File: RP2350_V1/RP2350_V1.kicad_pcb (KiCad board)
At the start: 4 copper layers, 65.3 x 95.8 mm, 102 parts, among them IC1 DMP1045U-7, IC2 DMP1045U-7, IC3 DMP1045U-7, J1 Conn_01x04_Pin, J2 Conn_01x08_Socket, J3 USB_C_Receptacle_USB2.0_16P, J4 Conn_01x08_Socket, J5 Conn_01x08_Socket, J6 Conn_01x02_Pin, J7 Conn_01x04_Pin, SW1 PTS 647 SN50 SMTR2 LFS, SW10 PTS 647 SN50 SMTR2 LFS, SW11 PTS 647 SN50 SMTR2 LFS, SW12 PTS 647 SN50 SMTR2 LFS, SW13 PTS 647 SN50 SMTR2 LFS, SW14 PTS 647 SN50 SMTR2 LFS, SW4 PTS 647 SN50 SMTR2 LFS, SW9 PTS 647 SN50 SMTR2 LFS, U1 RP2350_60QFN, U2 W25Q128JVS, U3 TPS628110AQWRWYRQ1, U4 MCP73812T-420I-OT, U5 TLV3012AIDBVR, U6 74HC14, Y1 ASE-12.000MHZ-ET

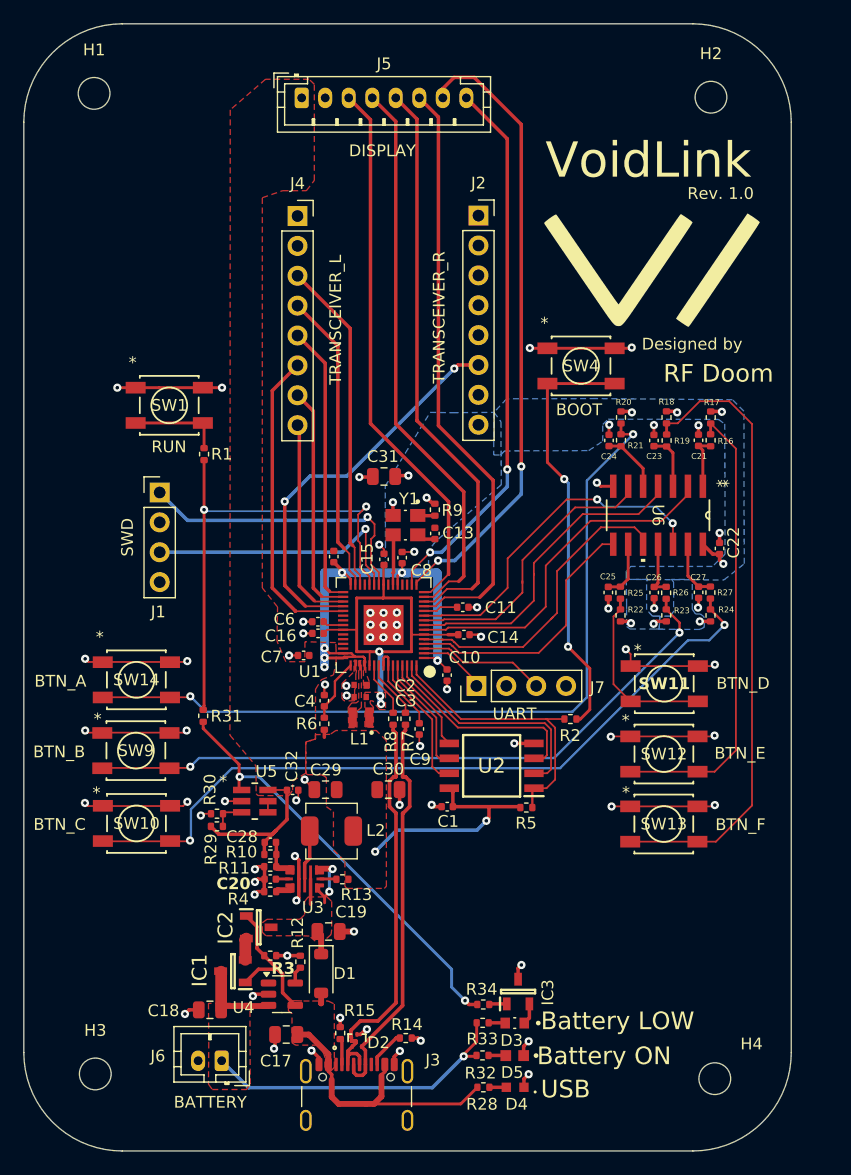
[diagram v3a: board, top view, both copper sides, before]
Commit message: sch updates, lay in progress
updated TLV3012 package,
changed cmos oscillator to xtal,
updated LCSC component values for all non-generic components
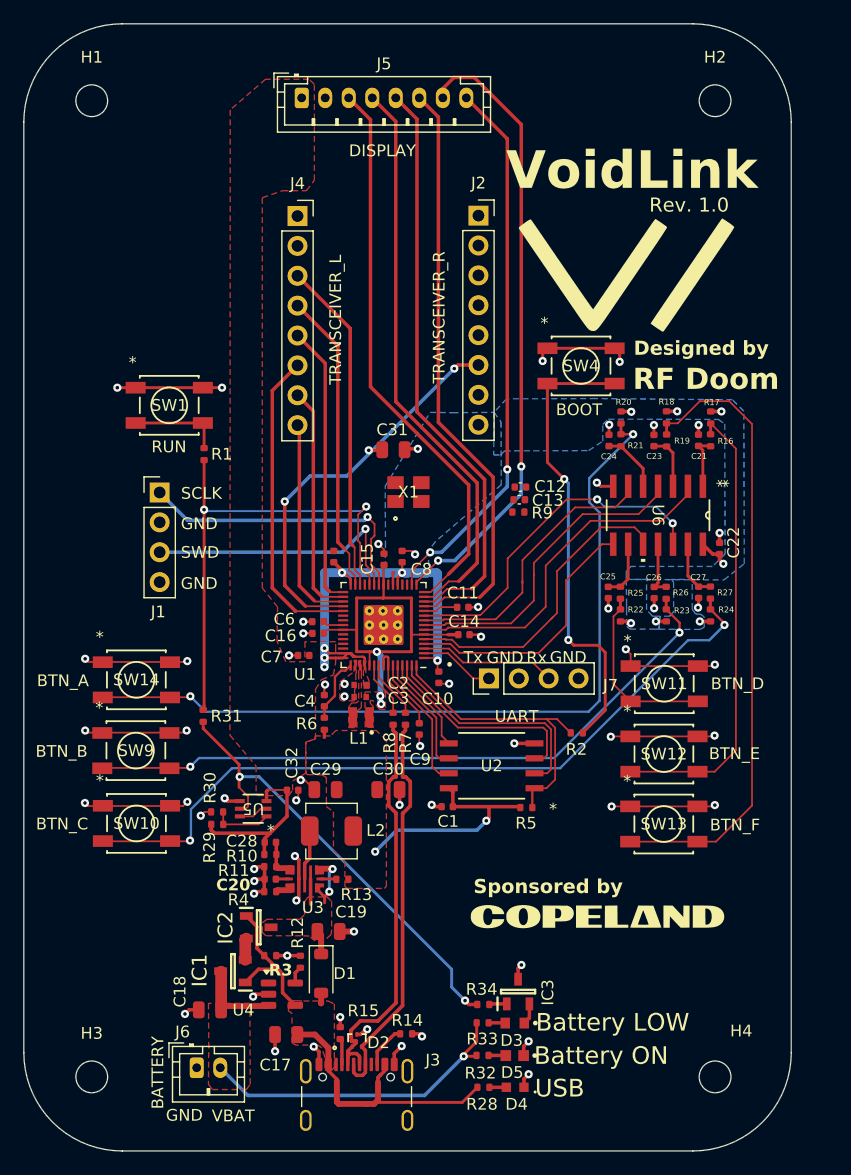
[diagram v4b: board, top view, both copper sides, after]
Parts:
- removed Y1: ASE-12.000MHZ-ET, My_Footprints:XTAL_ASE-12.000MHZ-ET
- added ?: , clipboard:0d6e4b69-4cda-4f93-960e-84a3754837eb, F.Cu at (150.4, 85.9)
- added C12: 15p, Capacitor_SMD:C_0402_1005Metric, F.Cu at (156.4, 70.8)
- added G***: LOGO, LOGO, F.Cu at (163.0, 107.4)
- added X1: ABM8-272-T3, My_Footprints:ABM8-272-T3_ABR, F.Cu at (146.9, 71.3)
- C13: value 1u -> 15p
- L2: value 0.47u -> 560n
- R9: value 10k -> 1k
- U1: footprint My_Footprints:RP2350A_QFN-60_EP_7.75x7.75_Pitch0.4mm -> My_Footprints:RP2350-QFN-60-1EP_7x7_P0.4mm_EP3.4x3.4mm_ThermalVias_NEW
- U2: footprint My_Footprints:SOIC127P790X216-8N -> My_Footprints:SOIC_128JVSIQ_WIN
- U3: value TPS628110AQWRWYRQ1 -> TPS62811QWRWYRQ1
- U5: value TLV3012AIDBVR -> TLV3012AIDCKR; footprint My_Footprints:DBV6 -> My_Footprints:DCK6
- moved C13 7.73 mm to (156.3, 71.9), turned to 0 degrees
- moved R9 7.10 mm to (156.3, 73.0), turned to 0 degrees
- moved C31 2.41 mm to (145.7, 67.7)
- moved G*** 2.20 mm to (165.5, 52.9)
- moved J6 2.20 mm to (128.9, 120.2), turned to 0 degrees
- moved R2 1.29 mm to (161.2, 91.8)
- moved J7 1.24 mm to (153.8, 87.1)
- moved C10 0.72 mm to (149.5, 87.0)
- moved U5 0.66 mm to (133.7, 98.2), turned to 180 degrees
- moved H1 0.66 mm to (120.0, 38.0)
- moved H2 0.46 mm to (173.0, 38.0)
- moved H3 0.39 mm to (120.0, 121.0)
- moved R14 0.36 mm to (146.7, 117.3)
- moved R29 0.17 mm to (130.7, 99.5)
- moved R30 0.16 mm to (130.7, 98.5)
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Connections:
- C13 pad 1: +3V3 -> /XIN
- J6 pad 1: /VBAT -> GND
- J6 pad 2: GND -> /VBAT
- R29 pad 2: Net-(U5-IN+) -> Net-(U5-OUT)
- R30 pad 1: Net-(U5-IN+) -> Net-(U5-OUT)
- R9 pad 1: +3V3 -> Net-(C12-Pad2)
- R9 pad 2: Net-(Y1-TRI-STATE(STBY)) -> /XOUT
- U1 pad 22: unconnected-(U1-XOUT-Pad22) -> /XOUT
- U5 pad 1: /UVLO_RST -> Net-(U5-OUT)
- U5 pad 2: GND -> Net-(U5-V+)
- U5 pad 3: Net-(U5-IN+) -> +3V3
- U5 pad 4: Net-(U5-IN-) -> GND
- U5 pad 5: Net-(U5-IN-) -> /UVLO_RST
- U5 pad 6: +3V3 -> Net-(U5-V+)
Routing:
- net Net-(U5-OUT): track 0.00 -> 5.21 mm
- net /XIN: track 4.27 -> 1.06 mm
- net /~{USB_BOOT}: track 36.4 -> 39.5 mm
- net Net-(U5-IN+): track 2.71 -> 0.00 mm
- net Net-(U5-V+): track 0.00 -> 2.54 mm
- net +3V3: track 98.1 -> 95.7 mm, vias 17 -> 16
- net /UVLO_RST: track 36.3 -> 38.7 mm
- net Net-(R20-Pad2): track 68.4 -> 69.9 mm
- net Net-(Y1-TRI-STATE(STBY)): track 1.47 -> 0.00 mm
- net /SPI1_TX: track 46.7 -> 48.1 mm
- net /QSPI_SS: track 24.2 -> 25.2 mm
- net Net-(U5-IN-): track 0.95 -> 0.00 mm
- net /SPI1_CLK: track 48.0 -> 49.0 mm
- net GND: track 124.5 -> 125.3 mm, vias 72 -> 62
- net /UART_Tx_DEBUG: track 5.82 -> 6.41 mm
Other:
- board text added: "GND"
- board text added: "Rx"
- board text added: "SCLK"
- board text added: "Sponsored by"
- board text added: "Tx"
- board text added: "VBAT"

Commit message: xtal lay done, JLC_DFM clean
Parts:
- moved C12 11.1 mm to (145.9, 74.3)
- moved R9 10.4 mm to (146.3, 75.9), turned to -90 degrees
- moved C13 8.34 mm to (148.3, 74.3)
- moved C8 2.15 mm to (148.5, 77.3), turned to 0 degrees
- moved X1 1.21 mm to (147.8, 72.0), turned to -90 degrees
- moved C15 0.73 mm to (144.4, 76.4)
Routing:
- net GND: track 125.3 -> 150.7 mm, vias 62 -> 68
- net /XIN: track 1.06 -> 9.36 mm
- net /XOUT: track 0.00 -> 3.29 mm
- net Net-(C12-Pad2): track 0.00 -> 2.97 mm
- net /DISPLAY_BUSY: track 46.8 -> 47.9 mm
- net /SWD: track 23.4 -> 24.4 mm
- net /SWCLK: track 25.2 -> 26.0 mm
- net +1V1: track 34.2 -> 35.0 mm
- net +3V3: track 95.7 -> 95.9 mm, vias 16 -> 15

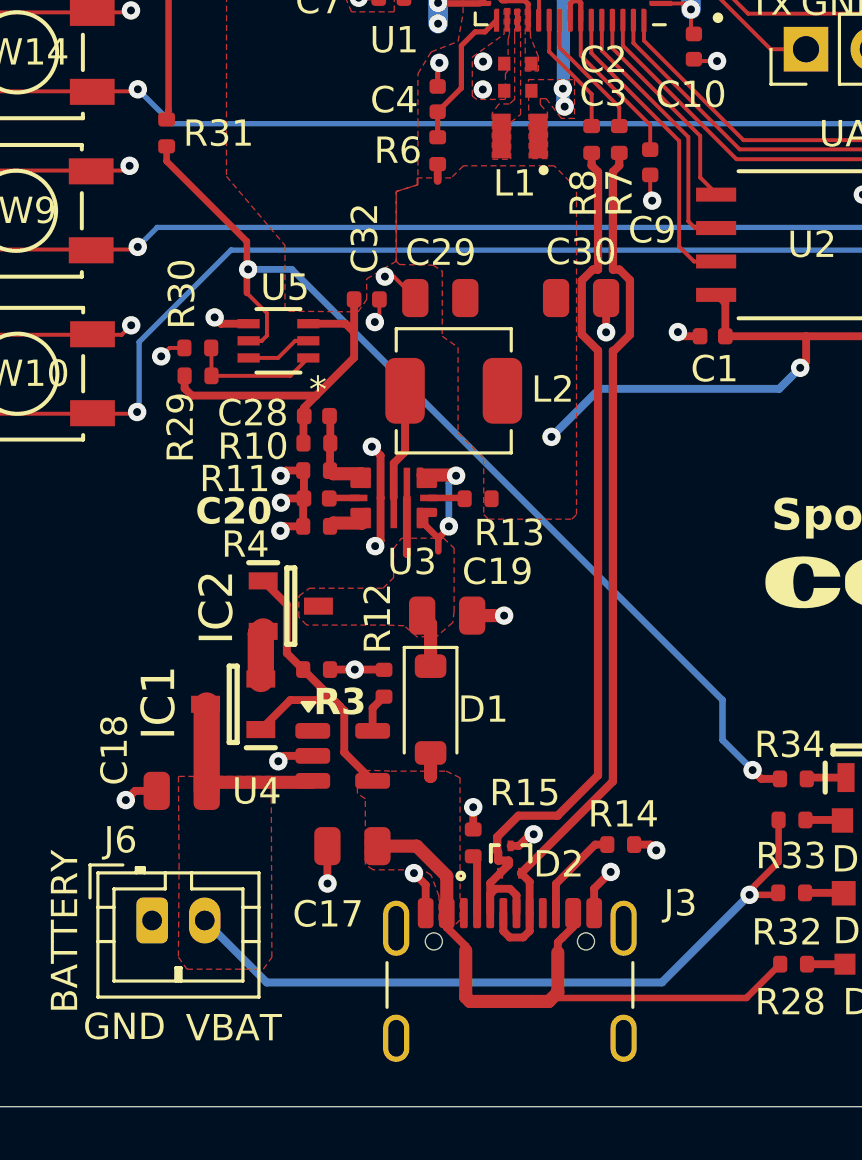
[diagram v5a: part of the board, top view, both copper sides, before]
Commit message: DONOT USE PREVIOUS VERSIONS! *Fixed TLV3012*, added TVS diodes
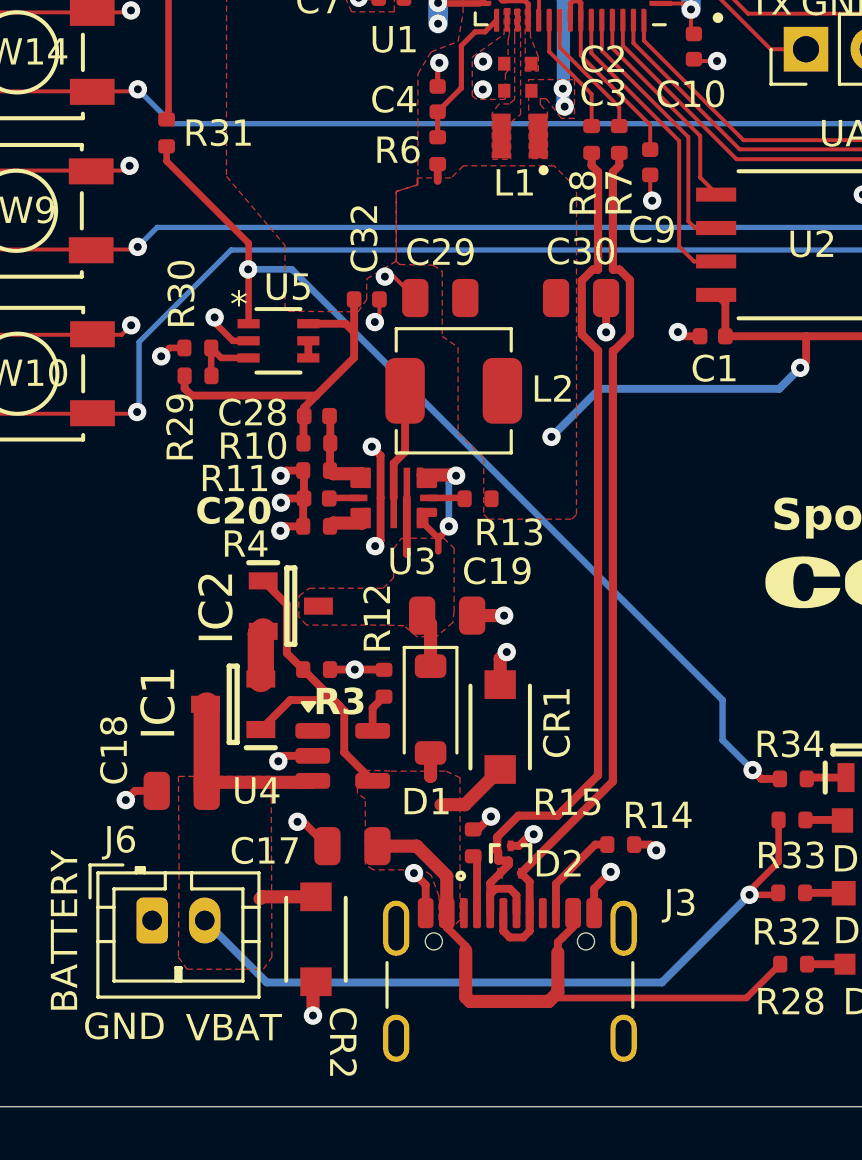
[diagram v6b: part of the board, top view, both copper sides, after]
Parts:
- added CR1: SMF12A, My_Footprints:SMFSeries_SOD-123F, F.Cu at (142.2, 112.9)
- added CR2: SMF12A, My_Footprints:SMFSeries_SOD-123F, F.Cu at (135.2, 120.9)
- turned U5 to 0 degrees
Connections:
- R29 pad 2: Net-(U5-OUT) -> Net-(U5-IN+)
- R30 pad 1: Net-(U5-OUT) -> Net-(U5-IN+)
- U5 pad 1: Net-(U5-OUT) -> /UVLO_RST
- U5 pad 2: Net-(U5-V+) -> GND
- U5 pad 3: +3V3 -> Net-(U5-IN+)
- U5 pad 4: GND -> Net-(U5-IN-)
- U5 pad 5: /UVLO_RST -> Net-(U5-IN-)
- U5 pad 6: Net-(U5-V+) -> +3V3
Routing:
- net Net-(U5-OUT): track 5.21 -> 0.00 mm
- net GND: track 150.7 -> 154.1 mm, vias 68 -> 70
- net Net-(U5-IN+): track 0.00 -> 2.83 mm
- net VBUS: track 38.1 -> 40.9 mm
- net /VBAT: track 34.9 -> 37.5 mm
- net Net-(U5-V+): track 2.54 -> 0.00 mm
- net /UVLO_RST: track 38.7 -> 37.2 mm
- net Net-(U5-IN-): track 0.00 -> 0.65 mm

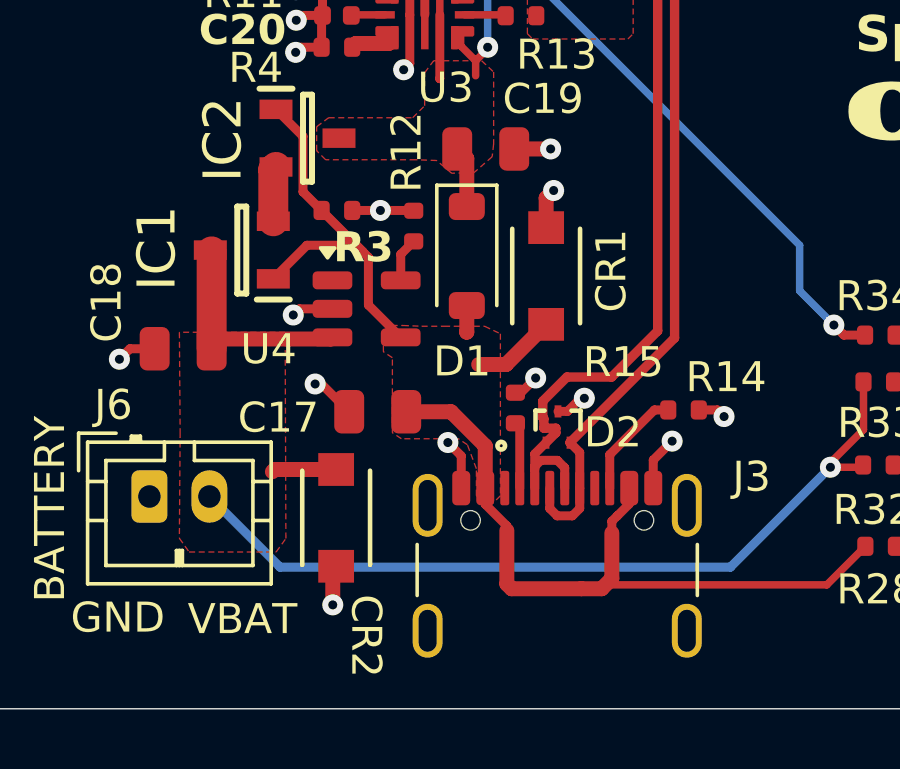
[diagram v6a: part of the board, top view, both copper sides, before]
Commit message: Updated TVS diode to bi-directional version (SMF12CA)
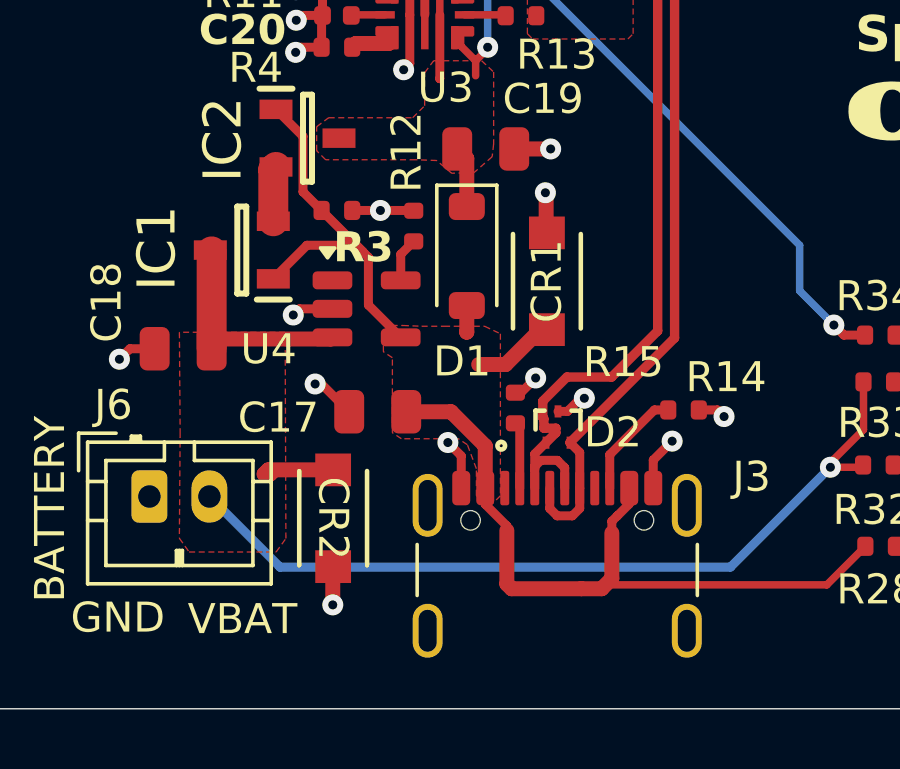
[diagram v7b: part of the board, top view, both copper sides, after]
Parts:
- CR1, CR2: value SMF12A -> SMF12CA
- moved CR1 0.18 mm to (142.2, 113.0)
- moved CR2 0.10 mm to (135.1, 121.0)

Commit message: updated LED resistors, re-exported fabrication outputs
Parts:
- R28: value 100 -> 85
- R32: value 120 -> 73.3
- R33: value 120 -> 88
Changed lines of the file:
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@@
 			)
 		)
-		(property "Value" "100"
+		(property "Value" "85"
 			(at 0 1.17 0)
 			(layer "F.Fab")
@@
 			)
 		)
-		(property "Value" "120"
+		(property "Value" "73.3"
 			(at 0 1.17 0)
 			(layer "F.Fab")
@@
 			)
 		)
-		(property "Value" "120"
+		(property "Value" "88"
 			(at 0 1.17 0)
 			(layer "F.Fab")
